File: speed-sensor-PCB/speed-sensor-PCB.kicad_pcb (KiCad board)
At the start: 2 copper layers, 33.8 x 40.5 mm, 9 parts, among them IC1 AS5600-ASOT, J1 Conn_01x01_Pin, J4 Conn_01x01_Pin, J5 Conn_01x01_Pin

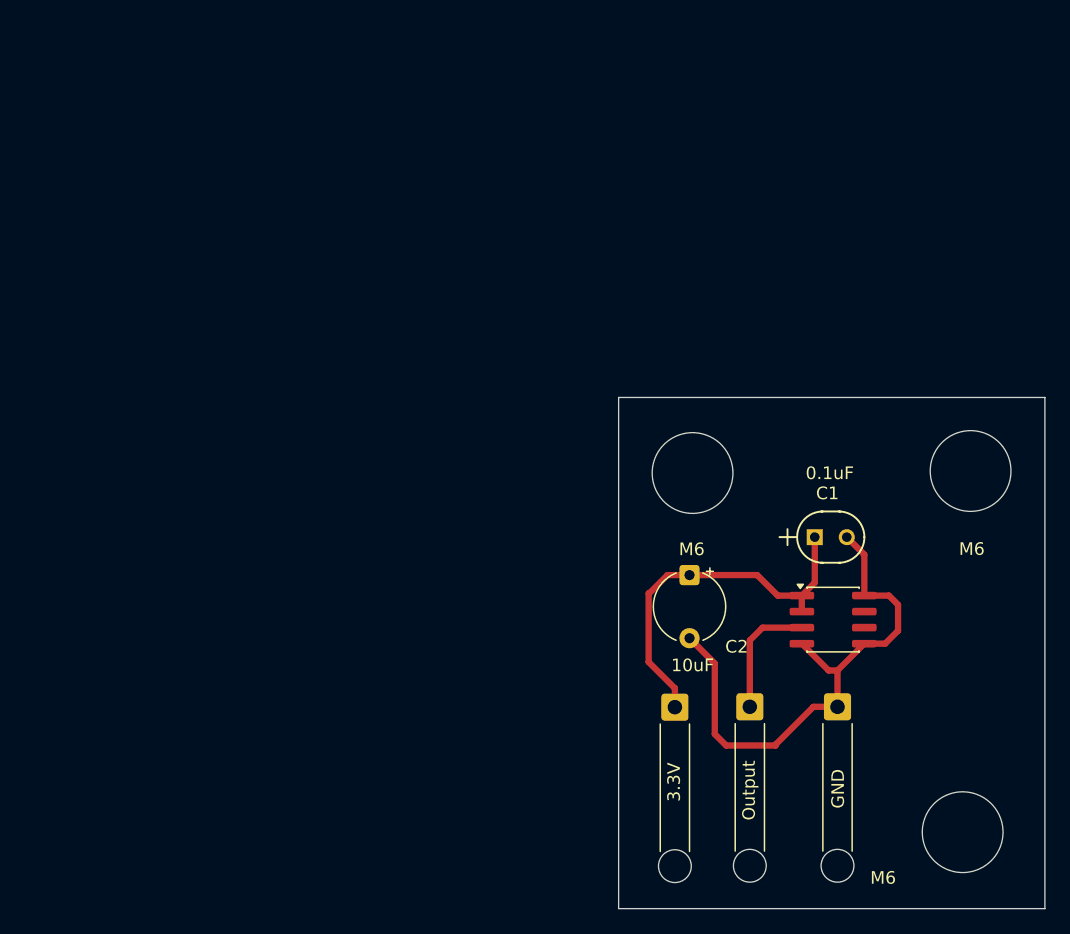
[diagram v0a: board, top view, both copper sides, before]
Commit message: ordered JST VH and made speed sensor PCB design
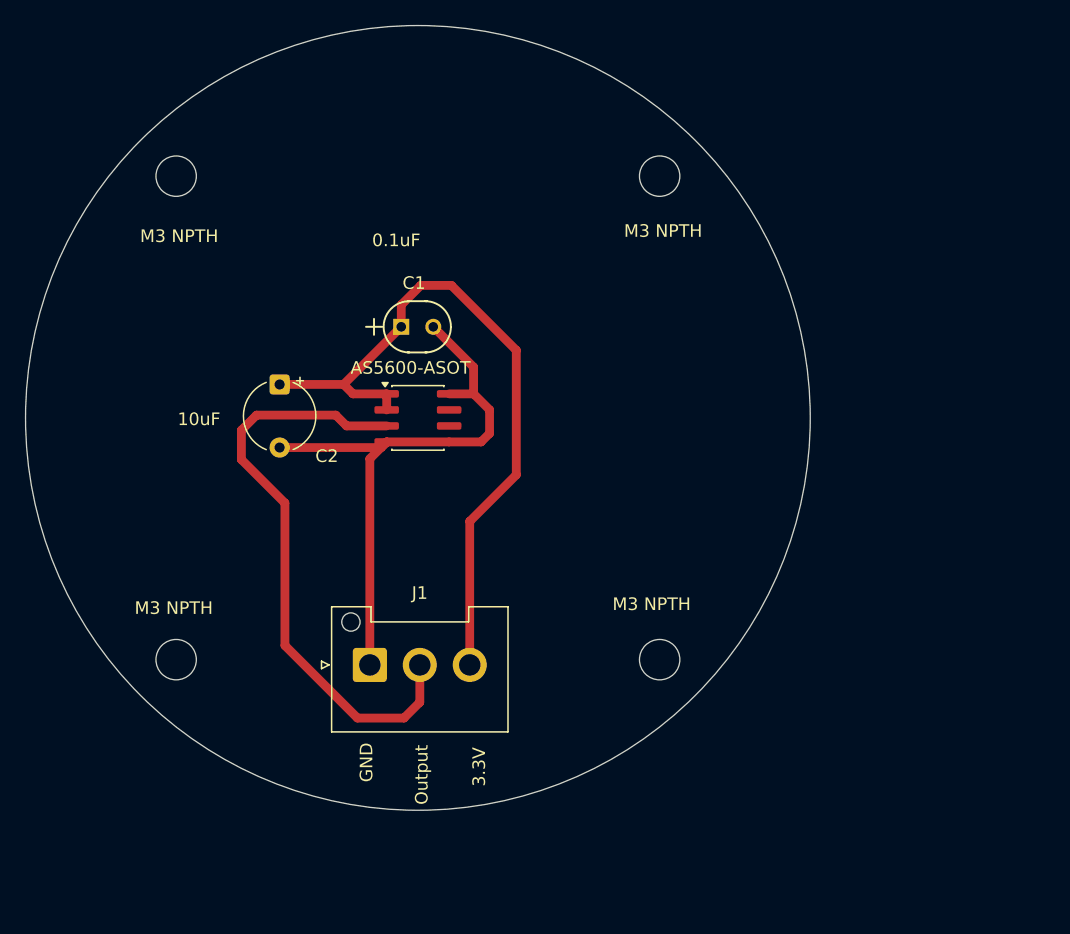
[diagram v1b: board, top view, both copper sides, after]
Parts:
- removed J4, J5: Conn_01x01_Pin, Connector_Wire:SolderWire-0.5sqmm_1x01_D0.9mm_OD2.1mm_Relief
- added H4: MountingHole, MountingHole:MountingHole_3.2mm_M3_ISO7380, F.Cu at (80.8, 80.8)
- H1, H2, H3: footprint MountingHole:MountingHole_6.4mm_M6_ISO14580 -> MountingHole:MountingHole_3.2mm_M3_ISO7380
- J1: value Conn_01x01_Pin -> Conn_01x03_Pin; footprint Connector_Wire:SolderWire-0.5sqmm_1x01_D0.9mm_OD2.1mm_Relief -> Connector_JST:JST_VH_B3P-VH-FB-B_1x03_P3.96mm_Vertical
- moved H2 64.7 mm to (80.8, 119.2)
- moved C1 36.8 mm to (98.7, 92.8)
- moved IC1 36.6 mm to (100.0, 100.0)
- moved C2 35.8 mm to (89.0, 97.3)
- moved H1 27.6 mm to (119.2, 119.2)
- moved J1 24.4 mm to (96.2, 119.6)
- moved H3 23.7 mm to (119.2, 80.8)
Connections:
- J1 pad 1: +3.3V -> GND
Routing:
- net Net-(IC1-OUT): track 9.81 -> 47.4 mm
- net +3.3V: track 29.6 -> 56.6 mm
- net GND: track 42.8 -> 47.6 mm
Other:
- board size 33.8 x 40.5 mm -> 62.2 x 62.2 mm
- board text added: "AS5600-ASOT"
- board text added: "M3 NPTH"
- board text removed: "J1"
- board text removed: "M6"
